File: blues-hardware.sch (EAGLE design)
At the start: 3 parts, among them J1 MDT420E01001NOTECARD

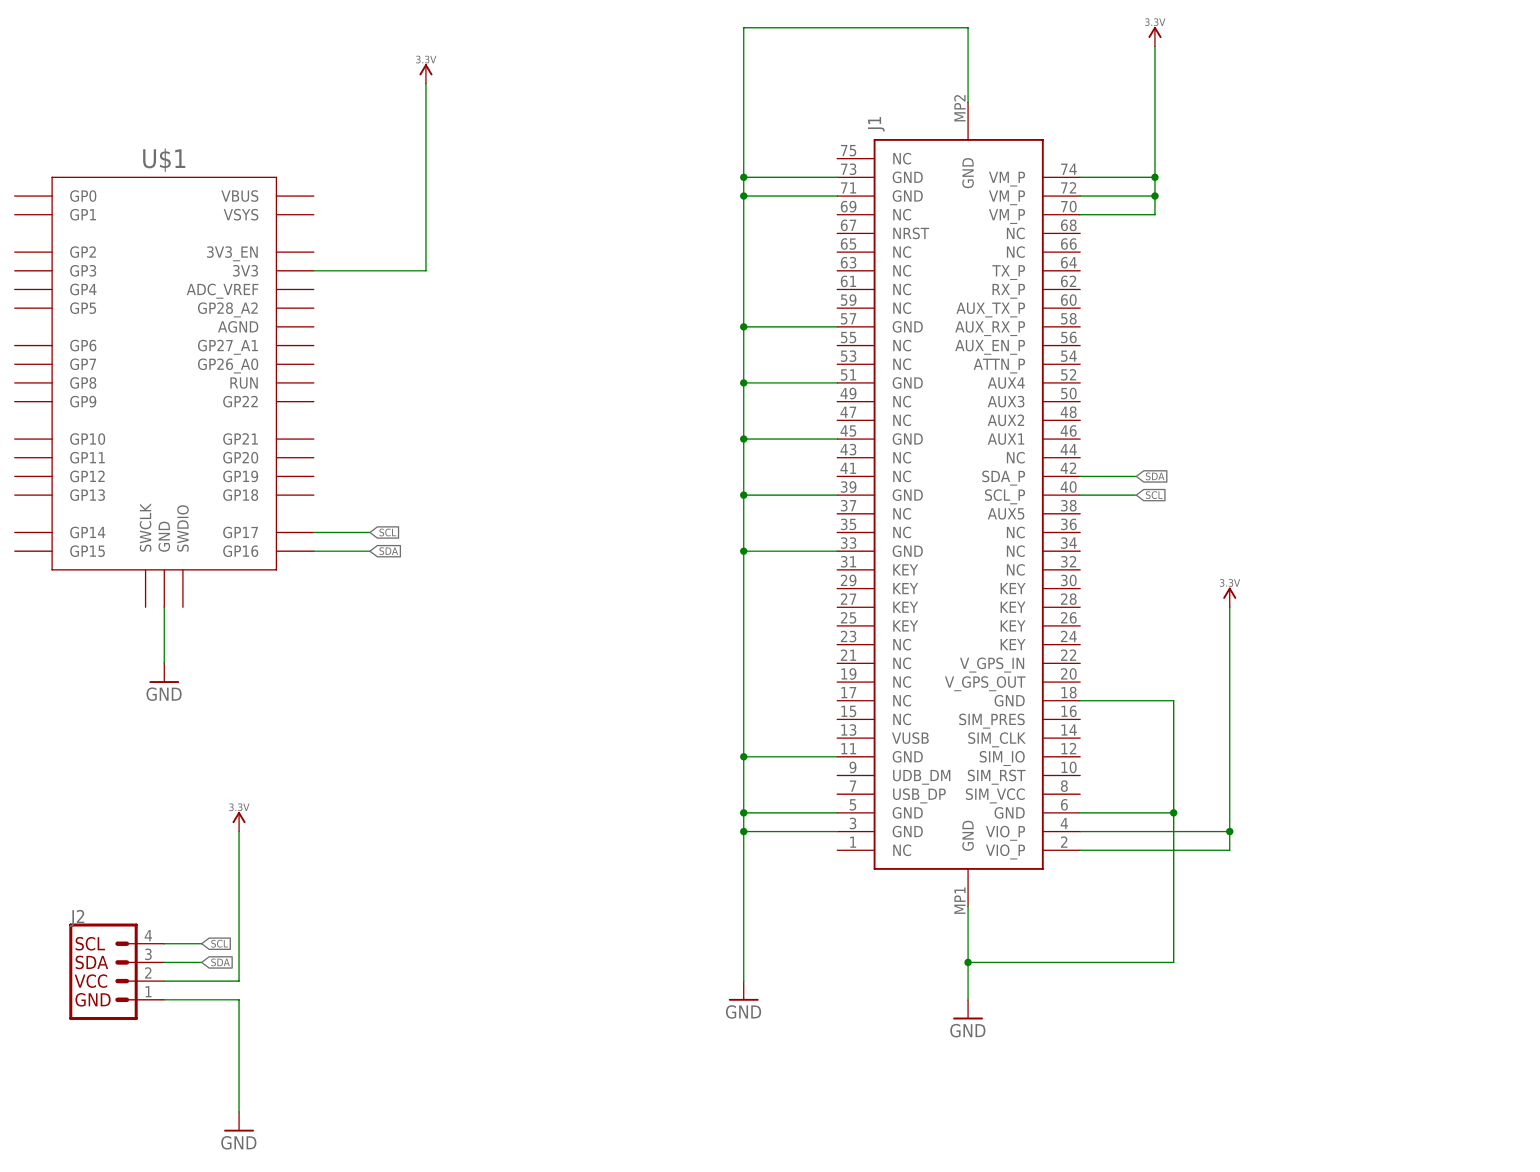
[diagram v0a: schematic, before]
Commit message: Changes to notecard library
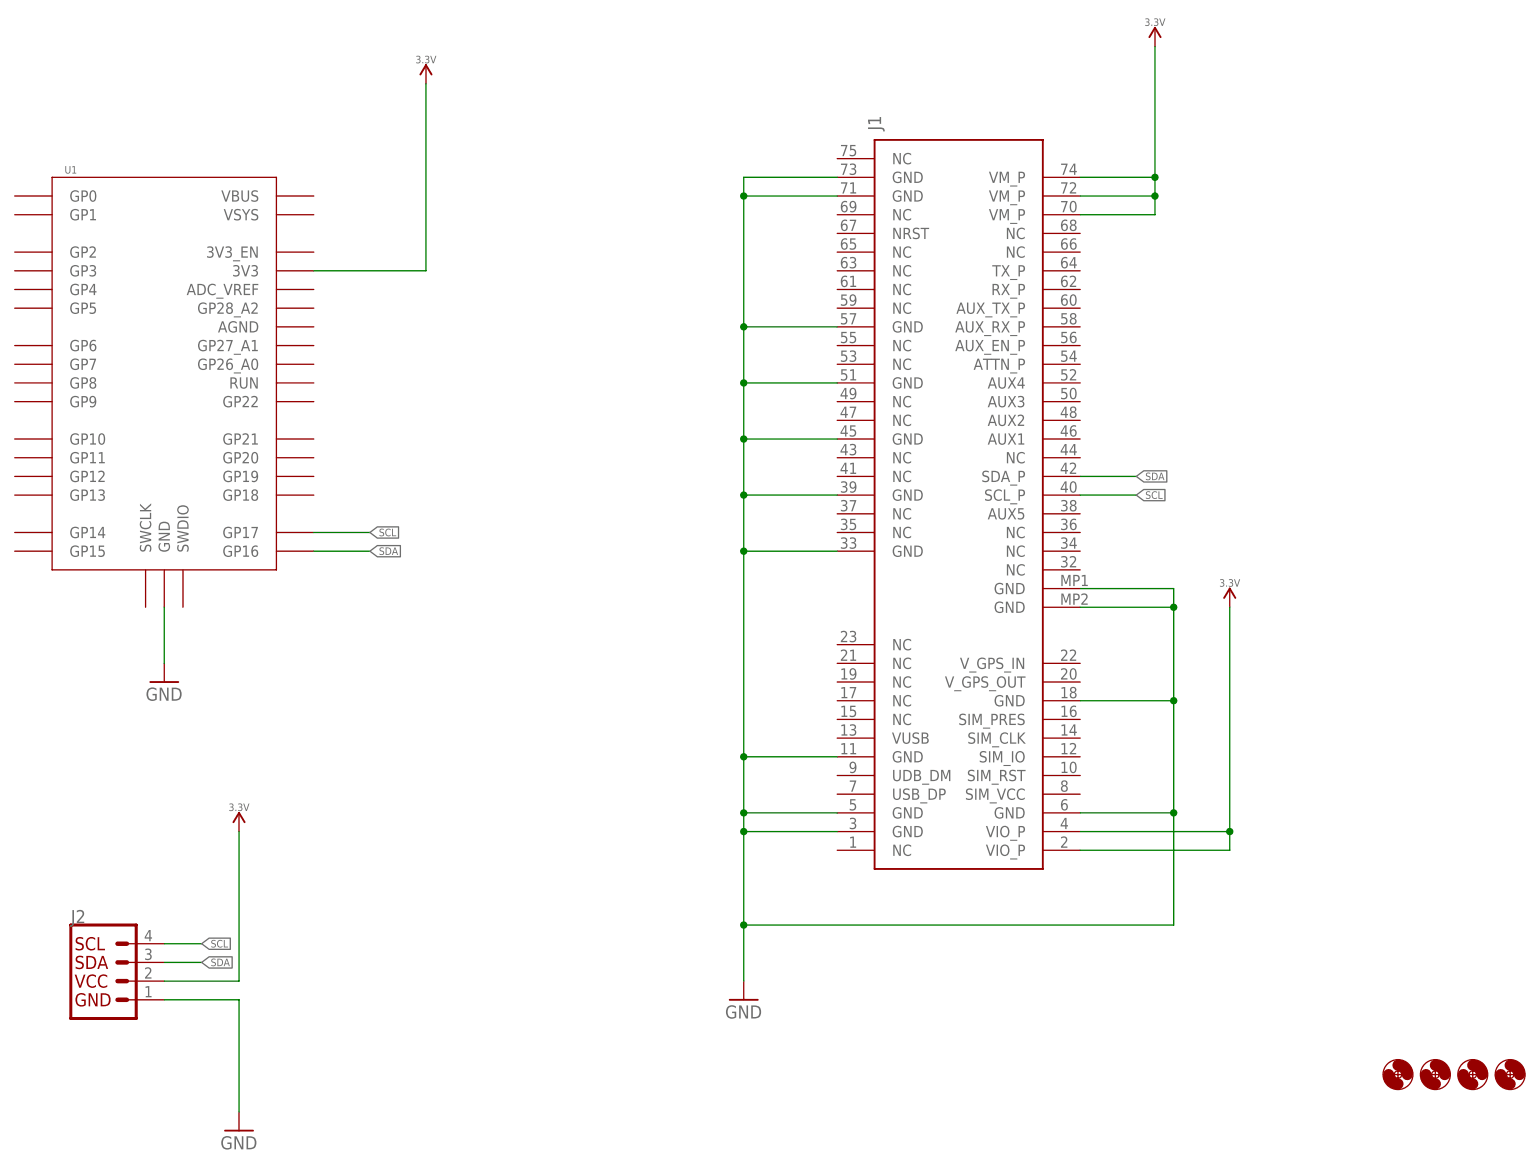
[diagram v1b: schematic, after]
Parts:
- added H1, H2, H3, H4: MOUNT-HOLE3.0, holes:MOUNT-HOLE3.0
- renumbered U$1 to U1
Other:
- note added: "Notecard"
- note added: "Qwiic"
- note added: "Raspberry Pi Pico"
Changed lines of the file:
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@@
 <?xml version="1.0" encoding="utf-8"?>
 <!DOCTYPE eagle SYSTEM "eagle.dtd">
-<eagle version="9.5.0">
+<eagle version="9.6.2">
 <drawing>
 <settings>
@@
 <layer number="115" name="ReferenceISLANDS" color="7" fill="1" visible="no" active="yes"/>
 <layer number="116" name="Patch_BOT" color="9" fill="4" visible="yes" active="yes"/>
+<layer number="117" name="PM_Ref" color="7" fill="1" visible="yes" active="yes"/>
 <layer number="118" name="Rect_Pads" color="7" fill="1" visible="no" active="yes"/>
+<layer number="119" name="PF_Ref" color="7" fill="1" visible="yes" active="yes"/>
+<layer number="120" name="WFL_Ref" color="7" fill="1" visible="yes" active="yes"/>
 <layer number="121" name="_tsilk" color="7" fill="1" visible="yes" active="yes"/>
 <layer number="122" name="_bsilk" color="7" fill="1" visible="yes" active="yes"/>
@@
 <parts>
 <part name="FRAME1" library="SparkFun-Aesthetics" library_urn="urn:adsk.eagle:library:507" deviceset="FRAME-A4L" device=""/>
-<part name="U$1" library="RaspberryPi_Pico" deviceset="RPI_PICO" device="-TH"/>
+<part name="U1" library="RaspberryPi_Pico" deviceset="RPI_PICO" device="-TH"/>
 <part name="J1" library="notecard" deviceset="MDT420E01001" device="NOTECARD"/>
 <part name="GND1" library="supply1" library_urn="urn:adsk.eagle:library:371" deviceset="GND" device=""/>
-<part name="GND2" library="supply1" library_urn="urn:adsk.eagle:library:371" deviceset="GND" device=""/>
 <part name="GND3" library="supply1" library_urn="urn:adsk.eagle:library:371" deviceset="GND" device=""/>
 <part name="SUPPLY1" library="SparkFun-PowerSymbols" library_urn="urn:adsk.eagle:library:530" deviceset="3.3V" device=""/>
@@
 <part name="SUPPLY3" library="SparkFun-PowerSymbols" library_urn="urn:adsk.eagle:library:530" deviceset="3.3V" device=""/>
 <part name="SUPPLY4" library="SparkFun-PowerSymbols" library_urn="urn:adsk.eagle:library:530" deviceset="3.3V" device=""/>
+<part name="H1" library="holes" library_urn="urn:adsk.eagle:library:237" deviceset="MOUNT-HOLE" device="3.0" package3d_urn="urn:adsk.eagle:package:14277/1"/>
+<part name="H2" library="holes" library_urn="urn:adsk.eagle:library:237" deviceset="MOUNT-HOLE" device="3.0" package3d_urn="urn:adsk.eagle:package:14277/1"/>
+<part name="H3" library="holes" library_urn="urn:adsk.eagle:library:237" deviceset="MOUNT-HOLE" device="3.0" package3d_urn="urn:adsk.eagle:package:14277/1"/>
+<part name="H4" library="holes" library_urn="urn:adsk.eagle:library:237" deviceset="MOUNT-HOLE" device="3.0" package3d_urn="urn:adsk.eagle:package:14277/1"/>
 </parts>
 <sheets>
 <sheet>
 <plain>
+<wire x1="116.84" y1="177.8" x2="116.84" y2="68.58" width="0.1524" layer="105" style="shortdash"/>
+<wire x1="116.84" y1="68.58" x2="0" y2="68.58" width="0.1524" layer="105" style="shortdash"/>
+<text x="22.86" y="154.94" size="6.4516" layer="105" font="vector" ratio="20">Raspberry Pi Pico</text>
+<text x="144.78" y="170.18" size="6.4516" layer="105" font="vector" ratio="20">Notecard</text>
+<text x="50.8" y="58.42" size="6.4516" layer="105" font="vector" ratio="20">Qwiic</text>
+<wire x1="116.84" y1="68.58" x2="116.84" y2="0" width="0.1524" layer="105" style="shortdash"/>
 </plain>
 <instances>
@@
 <attribute name="SHEET" x="195.58" y="1.27" size="2.54" layer="94" font="vector"/>
 </instance>
-<instance part="U$1" gate="G$1" x="63.5" y="116.84" smashed="yes">
-<attribute name="NAME" x="63.5" y="147.32" size="2.54" layer="95" align="center"/>
+<instance part="U1" gate="G$1" x="63.5" y="116.84" smashed="yes">
+<attribute name="NAME" x="50.8" y="145.796" size="1.016" layer="95" font="vector" ratio="20" align="center"/>
 <attribute name="VALUE" x="63.5" y="152.4" size="2.54" layer="95" align="center"/>
 </instance>
@@
 <attribute name="VALUE" x="60.96" y="73.66" size="1.778" layer="96"/>
 </instance>
-<instance part="GND2" gate="1" x="172.72" y="30.48" smashed="yes">
-<attribute name="VALUE" x="170.18" y="27.94" size="1.778" layer="96"/>
-</instance>
 <instance part="GND3" gate="1" x="142.24" y="33.02" smashed="yes">
 <attribute name="VALUE" x="139.7" y="30.48" size="1.778" layer="96"/>
@@
 <instance part="SUPPLY4" gate="G$1" x="208.28" y="86.36" smashed="yes">
 <attribute name="VALUE" x="208.28" y="89.154" size="1.016" layer="96" font="vector" ratio="20" align="bottom-center"/>
+</instance>
+<instance part="H1" gate="G$1" x="231.14" y="22.86" smashed="yes">
+<attribute name="NAME" x="233.172" y="23.4442" size="1.778" layer="95" display="off"/>
+<attribute name="VALUE" x="233.172" y="20.3962" size="1.778" layer="96" display="off"/>
+</instance>
+<instance part="H2" gate="G$1" x="236.22" y="22.86" smashed="yes">
+<attribute name="NAME" x="238.252" y="23.4442" size="1.778" layer="95" display="off"/>
+<attribute name="VALUE" x="238.252" y="20.3962" size="1.778" layer="96" display="off"/>
+</instance>
+<instance part="H3" gate="G$1" x="241.3" y="22.86" smashed="yes">
+<attribute name="NAME" x="243.332" y="23.4442" size="1.778" layer="95" display="off"/>
+<attribute name="VALUE" x="243.332" y="20.3962" size="1.778" layer="96" display="off"/>
+</instance>
+<instance part="H4" gate="G$1" x="246.38" y="22.86" smashed="yes">
+<attribute name="NAME" x="248.412" y="23.4442" size="1.778" layer="95" display="off"/>
+<attribute name="VALUE" x="248.412" y="20.3962" size="1.778" layer="96" display="off"/>
 </instance>
 </instances>
@@
 <segment>
 <pinref part="GND1" gate="1" pin="GND"/>
-<pinref part="U$1" gate="G$1" pin="GND"/>
+<pinref part="U1" gate="G$1" pin="GND"/>
 <wire x1="63.5" y1="78.74" x2="63.5" y2="86.36" width="0.1524" layer="91"/>
-</segment>
-<segment>
-<pinref part="GND2" gate="1" pin="GND"/>
-<pinref part="J1" gate="G$1" pin="GND@1"/>
-<wire x1="172.72" y1="33.02" x2="172.72" y2="38.1" width="0.1524" layer="91"/>
-<pinref part="J1" gate="G$1" pin="GND@14"/>
-<wire x1="172.72" y1="38.1" x2="172.72" y2="45.72" width="0.1524" layer="91"/>
-<wire x1="187.96" y1="58.42" x2="200.66" y2="58.42" width="0.1524" layer="91"/>
-<wire x1="200.66" y1="58.42" x2="200.66" y2="38.1" width="0.1524" layer="91"/>
-<wire x1="200.66" y1="38.1" x2="172.72" y2="38.1" width="0.1524" layer="91"/>
-<junction x="172.72" y="38.1"/>
-<pinref part="J1" gate="G$1" pin="GND@13"/>
-<wire x1="187.96" y1="73.66" x2="200.66" y2="73.66" width="0.1524" layer="91"/>
-<wire x1="200.66" y1="73.66" x2="200.66" y2="58.42" width="0.1524" layer="91"/>
-<junction x="200.66" y="58.42"/>
 </segment>
 <segment>
@@
 <wire x1="142.24" y1="58.42" x2="142.24" y2="55.88" width="0.1524" layer="91"/>
 <pinref part="J1" gate="G$1" pin="GND@3"/>
-<wire x1="142.24" y1="55.88" x2="142.24" y2="35.56" width="0.1524" layer="91"/>
+<wire x1="142.24" y1="55.88" x2="142.24" y2="43.18" width="0.1524" layer="91"/>
+<wire x1="142.24" y1="43.18" x2="142.24" y2="35.56" width="0.1524" layer="91"/>
 <wire x1="154.94" y1="55.88" x2="142.24" y2="55.88" width="0.1524" layer="91"/>
 <junction x="142.24" y="55.88"/>
@@
 <wire x1="154.94" y1="142.24" x2="142.24" y2="142.24" width="0.1524" layer="91"/>
 <junction x="142.24" y="142.24"/>
+<pinref part="J1" gate="G$1" pin="GND@14"/>
+<wire x1="187.96" y1="58.42" x2="200.66" y2="58.42" width="0.1524" layer="91"/>
+<wire x1="200.66" y1="58.42" x2="200.66" y2="43.18" width="0.1524" layer="91"/>
+<pinref part="J1" gate="G$1" pin="GND@13"/>
+<wire x1="187.96" y1="73.66" x2="200.66" y2="73.66" width="0.1524" layer="91"/>
+<wire x1="200.66" y1="73.66" x2="200.66" y2="58.42" width="0.1524" layer="91"/>
+<junction x="200.66" y="58.42"/>
+<wire x1="200.66" y1="43.18" x2="142.24" y2="43.18" width="0.1524" layer="91"/>
+<junction x="142.24" y="43.18"/>
+<pinref part="J1" gate="G$1" pin="GND@1"/>
+<wire x1="187.96" y1="88.9" x2="200.66" y2="88.9" width="0.1524" layer="91"/>
+<wire x1="200.66" y1="88.9" x2="200.66" y2="86.36" width="0.1524" layer="91"/>
+<junction x="200.66" y="73.66"/>
 <pinref part="J1" gate="G$1" pin="GND@2"/>
-<wire x1="172.72" y1="154.94" x2="172.72" y2="165.1" width="0.1524" layer="91"/>
-<wire x1="172.72" y1="165.1" x2="142.24" y2="165.1" width="0.1524" layer="91"/>
-<wire x1="142.24" y1="165.1" x2="142.24" y2="144.78" width="0.1524" layer="91"/>
-<junction x="142.24" y="144.78"/>
+<wire x1="200.66" y1="86.36" x2="200.66" y2="73.66" width="0.1524" layer="91"/>
+<wire x1="187.96" y1="86.36" x2="200.66" y2="86.36" width="0.1524" layer="91"/>
+<junction x="200.66" y="86.36"/>
 </segment>
 <segment>
@@
 <net name="3.3V" class="0">
 <segment>
-<pinref part="U$1" gate="G$1" pin="3V3"/>
+<pinref part="U1" gate="G$1" pin="3V3"/>
 <pinref part="SUPPLY1" gate="G$1" pin="3.3V"/>
 <wire x1="83.82" y1="132.08" x2="99.06" y2="132.08" width="0.1524" layer="91"/>
@@
 <net name="SDA" class="0">
 <segment>
-<pinref part="U$1" gate="G$1" pin="GP16"/>
+<pinref part="U1" gate="G$1" pin="GP16"/>
 <wire x1="83.82" y1="93.98" x2="91.44" y2="93.98" width="0.1524" layer="91"/>
 <label x="91.44" y="93.98" size="1.016" layer="95" font="vector" ratio="20" xref="yes"/>
@@
 <net name="SCL" class="0">
 <segment>
-<pinref part="U$1" gate="G$1" pin="GP17"/>
+<pinref part="U1" gate="G$1" pin="GP17"/>
 <wire x1="83.82" y1="96.52" x2="91.44" y2="96.52" width="0.1524" layer="91"/>
 <label x="91.44" y="96.52" size="1.016" layer="95" font="vector" ratio="20" xref="yes"/>
